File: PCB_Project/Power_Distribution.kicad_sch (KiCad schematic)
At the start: 75 parts, among them J11 m1, J5 Power Connector, J6 s1, J7 s2, J8 s3, J9 s4

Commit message: working on pcb
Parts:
- renumbered 11 to 111, 111 to 1111, 1111 to 11111, 1111 to 11112, 1111 to 11113, 1111 to 11114, C17 to C12, C18 to C13, C19 to C14, C12 to C15, C13 to C16, C14 to C17, C20 to C18, C21 to C19, C15 to C20, C16 to C21, C37 to C27, C38 to C28, C39 to C29, C40 to C30, C41 to C31, C27 to C32, C28 to C33, C29 to C34, C30 to C35, C31 to C36, C32 to C37, C33 to C38, C34 to C39, C35 to C40, C36 to C41, D8 to D1, D11 to D10, D5 to D11, D6 to D12, D7 to D13, D1 to D2, D9 to D3, D12 to D4, D10 to D5, D13 to D6, D2 to D7, D3 to D8, D4 to D9, J11 to J10, L2 to L1, L1 to L2, L6 to L4, L4 to L5, L5 to L6, R24 to R10, R22 to R11, R25 to R12, R9 to R13, R23 to R14, R10 to R15, R11 to R16, R12 to R17, R13 to R18, R14 to R19, R8 to R6, R6 to R7, R7 to R8, R21 to R9

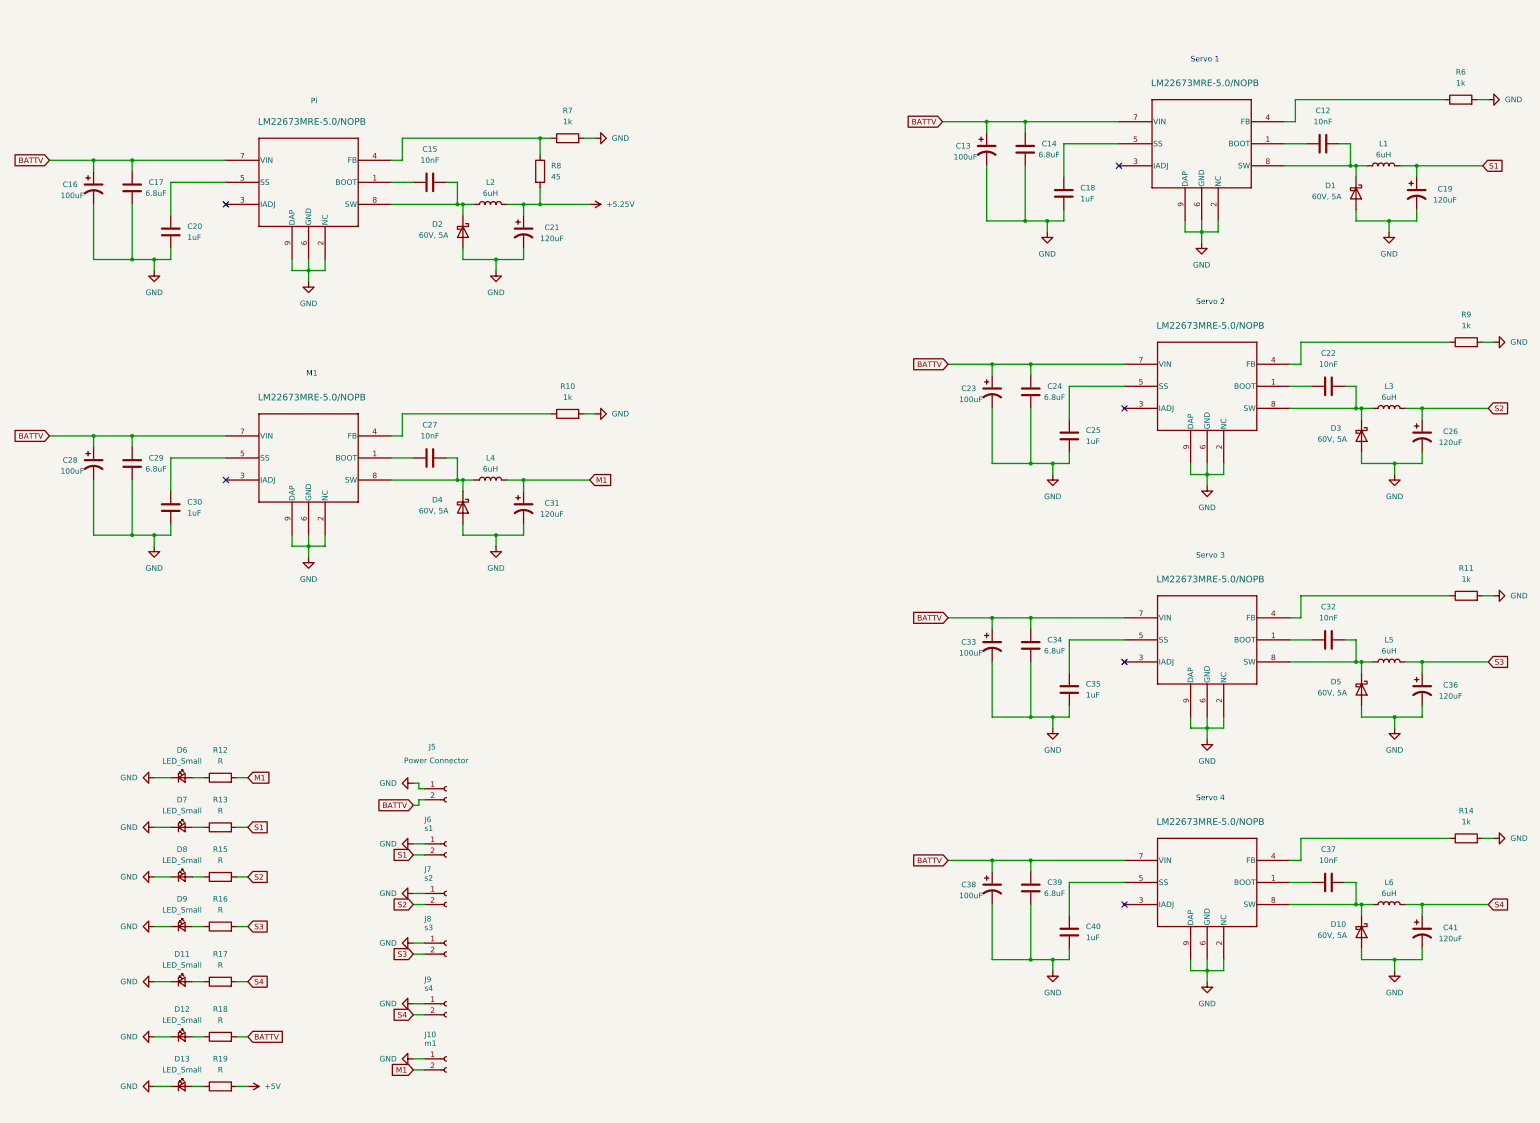
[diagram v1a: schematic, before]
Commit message: Swapped JST's and fixed FB connections
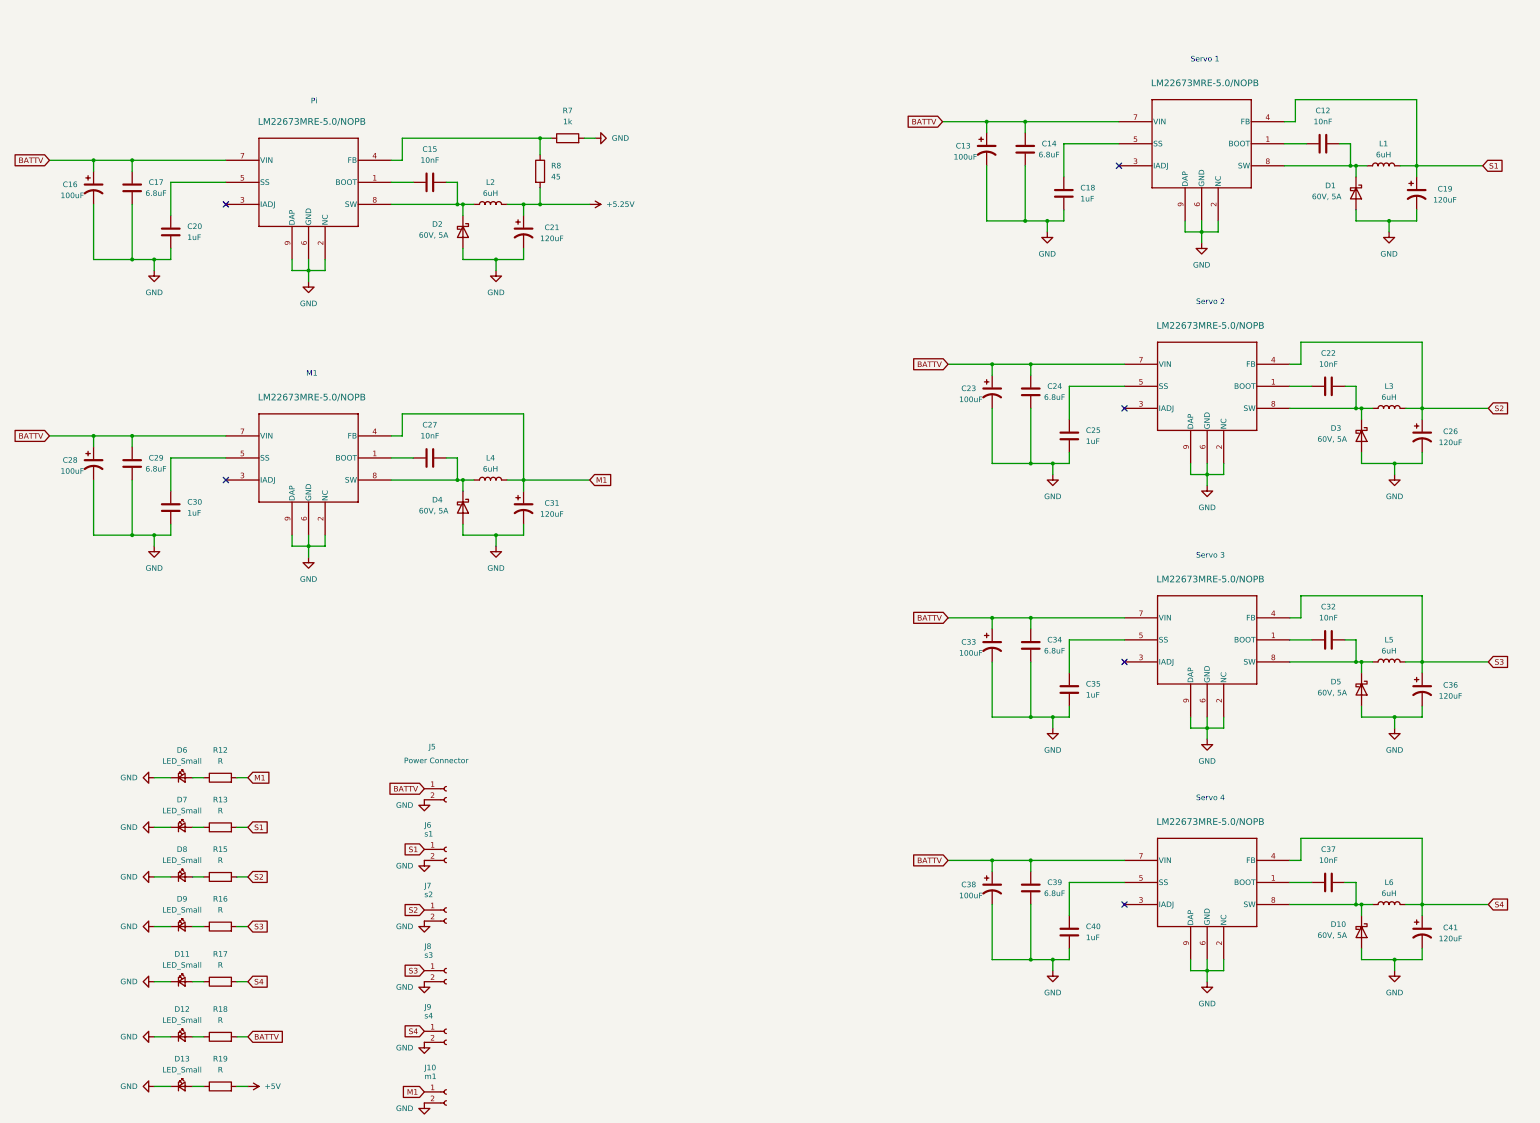
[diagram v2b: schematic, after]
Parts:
- removed R10, R11, R14, R6, R9: 1k, Resistor_SMD:R_0603_1608Metric, symbol Device:R
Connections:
- net BATTV: now also J5.1 (Pin_1); no longer J5.2 (Pin_2)
- net GND: now also J10.2 (Pin_2), J5.2 (Pin_2), J6.2 (Pin_2), J7.2 (Pin_2), J8.2 (Pin_2), J9.2 (Pin_2); no longer J10.1 (Pin_1), J5.1 (Pin_1), J6.1 (Pin_1), J7.1 (Pin_1), J8.1 (Pin_1), J9.1 (Pin_1)
- net M1: now also 11112.4 (FB), J10.1 (Pin_1); no longer J10.2 (Pin_2)
- net S1: now also 1111.4 (FB), J6.1 (Pin_1); no longer J6.2 (Pin_2)
- net S2: now also 11111.4 (FB), J7.1 (Pin_1); no longer J7.2 (Pin_2)
- net S3: now also 11113.4 (FB), J8.1 (Pin_1); no longer J8.2 (Pin_2)
- net S4: now also 11114.4 (FB), J9.1 (Pin_1); no longer J9.2 (Pin_2)
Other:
- moved on the sheet: J10, J6, J7, J8, J9

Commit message: finally
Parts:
- removed J6: s1, Connector_JST:JST_PH_B2B-PH-K_1x02_P2.00mm_Vertical, symbol Connector:Conn_01x02_Socket
- removed J7: s2, Connector_JST:JST_PH_B2B-PH-K_1x02_P2.00mm_Vertical, symbol Connector:Conn_01x02_Socket
- removed J8: s3, Connector_JST:JST_PH_B2B-PH-K_1x02_P2.00mm_Vertical, symbol Connector:Conn_01x02_Socket
- removed J9: s4, Connector_JST:JST_PH_B2B-PH-K_1x02_P2.00mm_Vertical, symbol Connector:Conn_01x02_Socket
- added J12, J13, J14, J6: Conn_01x03_Socket, Connector_JST:JST_PH_B3B-PH-K_1x03_P2.00mm_Vertical, symbol Connector:Conn_01x03_Socket
- C13, C16, C23, C28, C33, C38: footprint (none) -> Capacitor_SMD:CP_WCAP-PSHP
- C19, C21, C26, C31, C36, C41: footprint (none) -> Capacitor_SMD:CP_Elec_10x12.5
- D1, D10, D3, D4, D5: footprint (none) -> Diode_SMD:D_PowerDI-5
- D11, D12, D13, D6, D7, D8, D9: footprint LED_SMD:LED_0805_2012Metric -> Diode_SMD:D_0603_1608Metric
- D2: value 60V, 5A -> 15.6V, >3A; footprint (none) -> Diode_SMD:D_PowerDI-5
- J10: value m1 -> Motor Power Connection
- J5: value Power Connector -> Battery Connector
- L1, L2, L3, L4, L5, L6: footprint (none) -> Inductor_SMD:L_6.7x6.7mm
- R12, R13, R15, R16, R17, R19: value R -> 200
- R18: value R -> 800
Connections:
- net +5V is gone; now on net +5.25V: R19.2
- net GND: now also J12.3 (Pin_3), J13.3 (Pin_3), J14.3 (Pin_3), J6.3 (Pin_3)
- net S1: now also J12.2 (Pin_2)
- net S2: now also J6.2 (Pin_2)
- net S3: now also J13.2 (Pin_2)
- net S4: now also J14.2 (Pin_2)
- new net S1_PWM: J12.1 (Pin_1)
- new net S2_PWM: J6.1 (Pin_1)
- new net S3_PWM: J13.1 (Pin_1)
- new net S4_PWM: J14.1 (Pin_1)
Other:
- note added: "Motor 1"
- note added: "Servo Connections"
- note removed: "M1"
- moved on the sheet: J10
